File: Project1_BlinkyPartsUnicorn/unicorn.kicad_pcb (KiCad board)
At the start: 2 copper layers, 68.8 x 71.1 mm, 5 parts

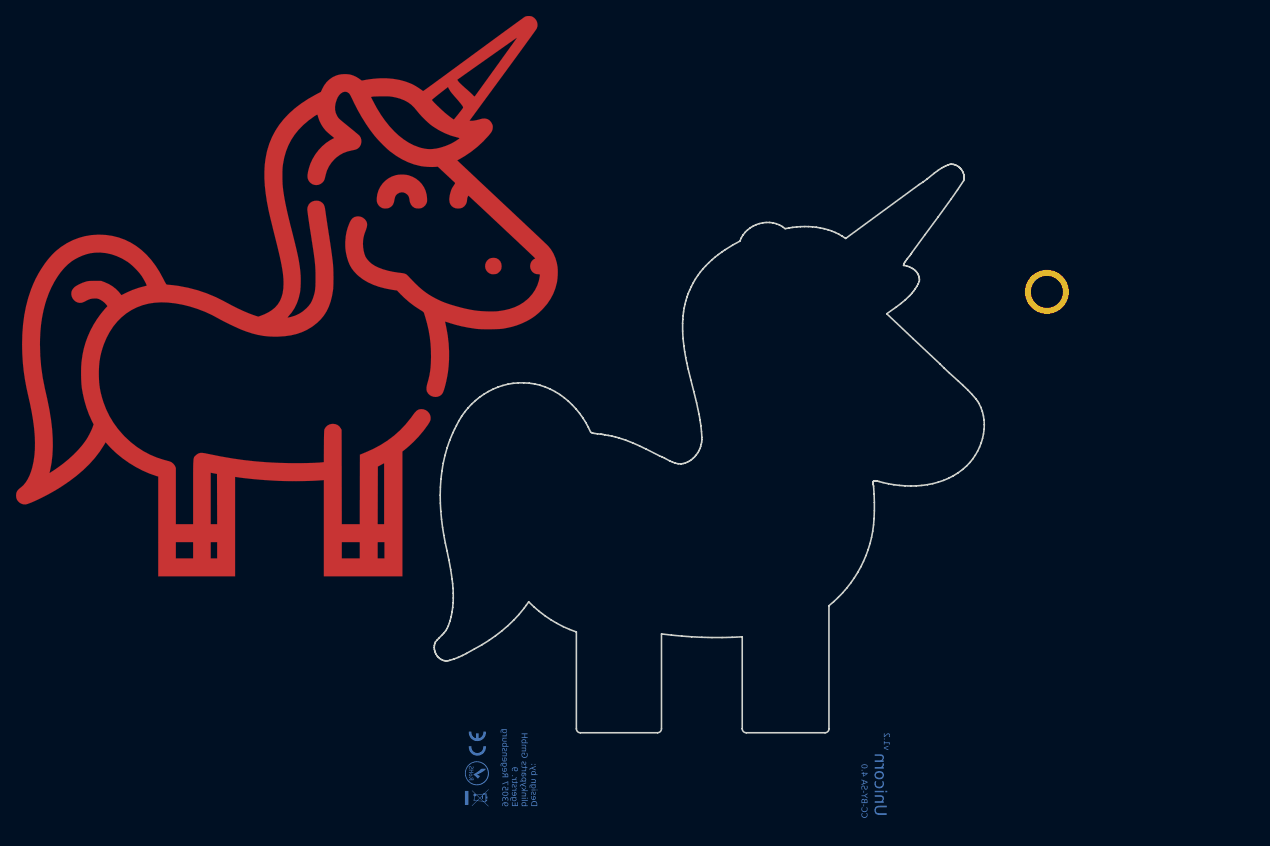
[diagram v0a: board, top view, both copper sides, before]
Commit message: Updating plan for Session 3
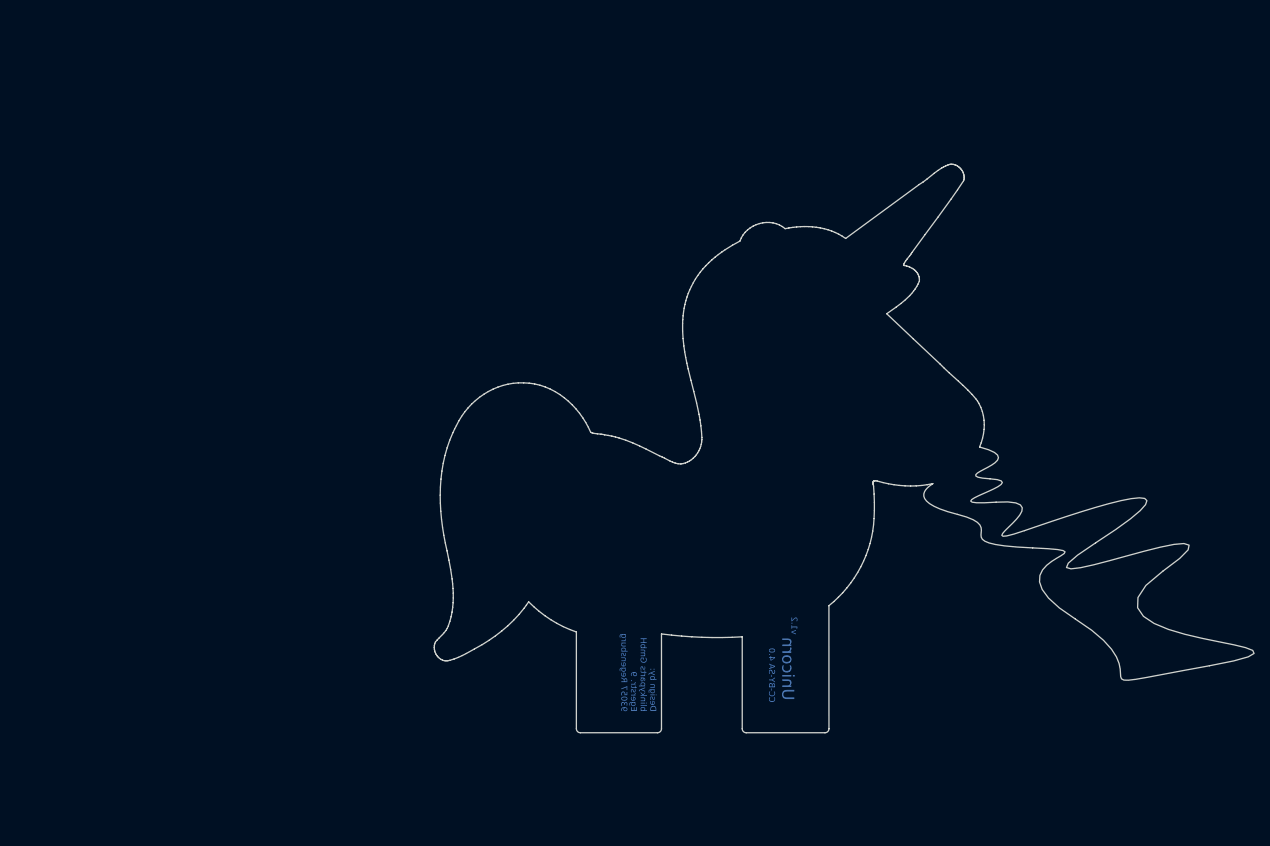
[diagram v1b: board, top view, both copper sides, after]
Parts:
- removed REF**: MountingHole_2.2mm_M2, MountingHole:MountingHole_2.2mm_M2
- removed Ref**: Val**, Binary_Kitchen:unicorn01
- removed ce_icon_mask_cu_3mm: G***, blinkyparts:ce-icon_Mask_Cu_3mm
- removed rohs_icon_mask_cu_3mm: G***, blinkyparts:rohs-icon_Mask_Cu_3mm
- removed weee_icon_mask_cu_3mm: G***, blinkyparts:weee-icon_Mask_Cu_3mm
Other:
- board size 68.8 x 71.1 mm -> 102.5 x 71.1 mm
